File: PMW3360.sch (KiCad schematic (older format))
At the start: 10 parts, among them J1 Conn_01x07, U1 PMW3360, U2 TCR2EF19

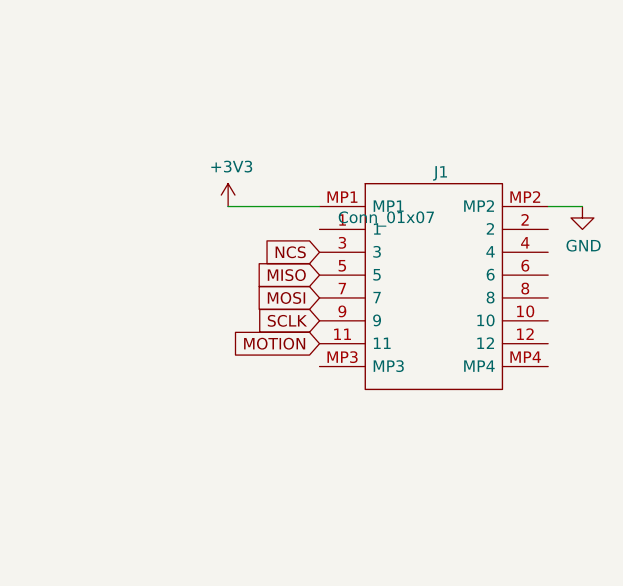
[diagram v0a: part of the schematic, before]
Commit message: Corrected the power lines - connected them to the right pins of the sockets.
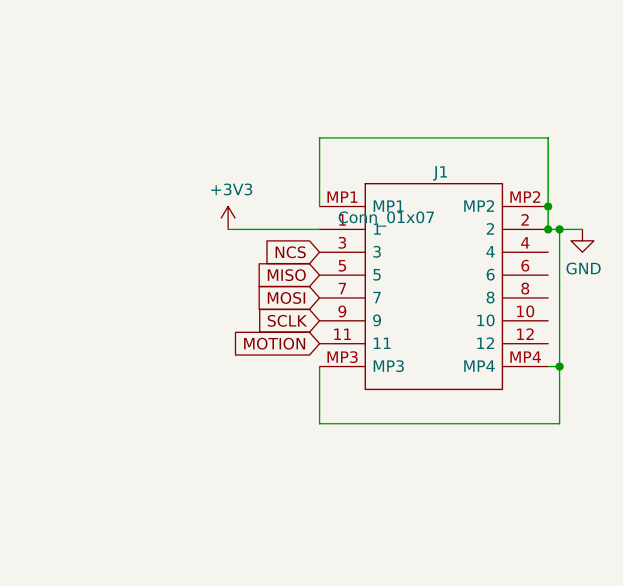
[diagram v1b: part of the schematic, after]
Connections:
- net +3V3: now also J1.1; no longer J1.MP1
- net GND: now also J1.2, J1.MP1, J1.MP3, J1.MP4
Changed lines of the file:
@@
 L power:+3V3 #PWR0108
 U 1 1 61215295
-P 8100 3900
-F 0 "#PWR0108" H 8100 3750 50  0001 C CNN
-F 1 "+3V3" H 8115 4073 50  0000 C CNN
-F 2 "" H 8100 3900 50  0001 C CNN
-F 3 "" H 8100 3900 50  0001 C CNN
-	1    8100 3900
+P 8100 4000
+F 0 "#PWR0108" H 8100 3850 50  0001 C CNN
+F 1 "+3V3" H 8115 4173 50  0000 C CNN
+F 2 "" H 8100 4000 50  0001 C CNN
+F 3 "" H 8100 4000 50  0001 C CNN
+	1    8100 4000
 	1    0    0    -1
 $EndComp
@@
 L power:GND #PWR0109
 U 1 1 6121663E
-P 9650 3900
-F 0 "#PWR0109" H 9650 3650 50  0001 C CNN
-F 1 "GND" H 9655 3727 50  0000 C CNN
-F 2 "" H 9650 3900 50  0001 C CNN
-F 3 "" H 9650 3900 50  0001 C CNN
-	1    9650 3900
+P 9650 4000
+F 0 "#PWR0109" H 9650 3750 50  0001 C CNN
+F 1 "GND" H 9655 3827 50  0000 C CNN
+F 2 "" H 9650 4000 50  0001 C CNN
+F 3 "" H 9650 4000 50  0001 C CNN
+	1    9650 4000
 	1    0    0    -1
 $EndComp
@@
 	2000 3750 2300 3750
 Wire Wire Line
-	9500 3900 9650 3900
+	9500 4000 9550 4000
 Wire Wire Line
-	8100 3900 8500 3900
+	8100 4000 8500 4000
 $Comp
 L Mechanical:MountingHole_Pad H1
@@
 	1    0    0    -1
 $EndComp
+Wire Wire Line
+	9500 3900 9500 4000
+Connection ~ 9500 4000
+Wire Wire Line
+	9500 4600 9550 4600
+Wire Wire Line
+	9550 4600 9550 4000
+Connection ~ 9550 4000
+Wire Wire Line
+	9550 4000 9650 4000
+Wire Wire Line
+	8500 4600 8500 4850
+Wire Wire Line
+	8500 4850 9550 4850
+Wire Wire Line
+	9550 4850 9550 4600
+Connection ~ 9550 4600
+Wire Wire Line
+	8500 3900 8500 3600
+Wire Wire Line
+	8500 3600 9500 3600
+Wire Wire Line
+	9500 3600 9500 3900
+Connection ~ 9500 3900
 $EndSCHEMATC
